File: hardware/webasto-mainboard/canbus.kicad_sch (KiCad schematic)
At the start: 17 parts, among them Q17 2N7002, Q18 2N7002, U10 MCP2557FD-xMF, U8 TCA9534, U9 MCP2517FD, X1 ASV-20.000MHZ-EJ-T

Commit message: Remove WiFi, plumb in the CANBus
- The next joy will be to remove the external I2C, and have all the
  sensors talk to us via CANBus as well.
- First I need to determine how to restructure to enumerate my sensors
- Nice thing is, the sensors will share an ID space across the bus
  (including LINBus, which will now need rework too)
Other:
- note added: "I2C Addr 0x20-27 We will use 27"
- note removed: "I2C Addr 0x38-3F We will use 3F"
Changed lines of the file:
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@@
     (stroke (width 0) (type default) (color 0 0 0 0))
   )
-  (text "I2C Addr 0x38-3F\nWe will use 3F" (at 61.087 182.753 0)
+  (text "I2C Addr 0x20-27\nWe will use 27" (at 61.087 182.753 0)
     (effects (font (size 1.27 1.27)) (justify left bottom))
   )

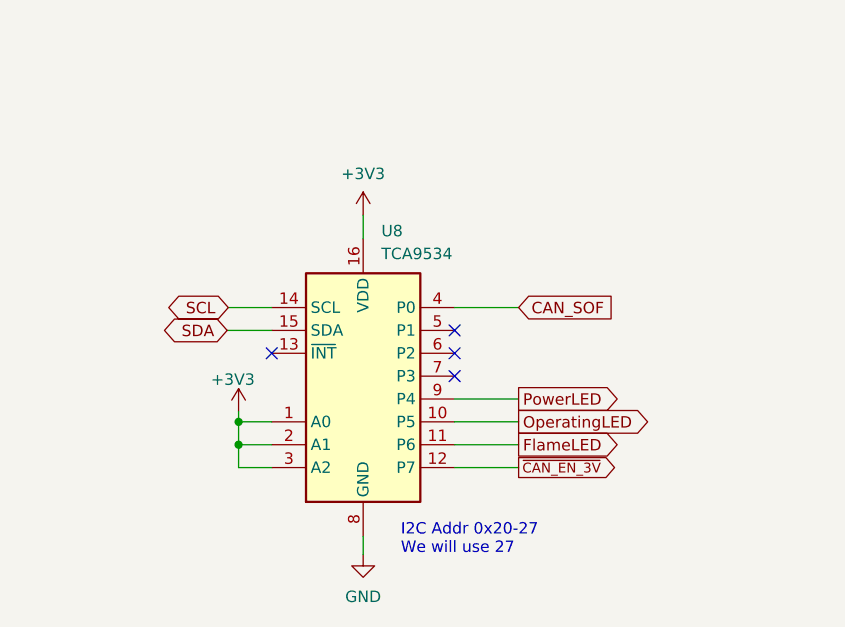
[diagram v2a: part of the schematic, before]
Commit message: Removing KLine and I2C from X1, reattaching the external IOs.
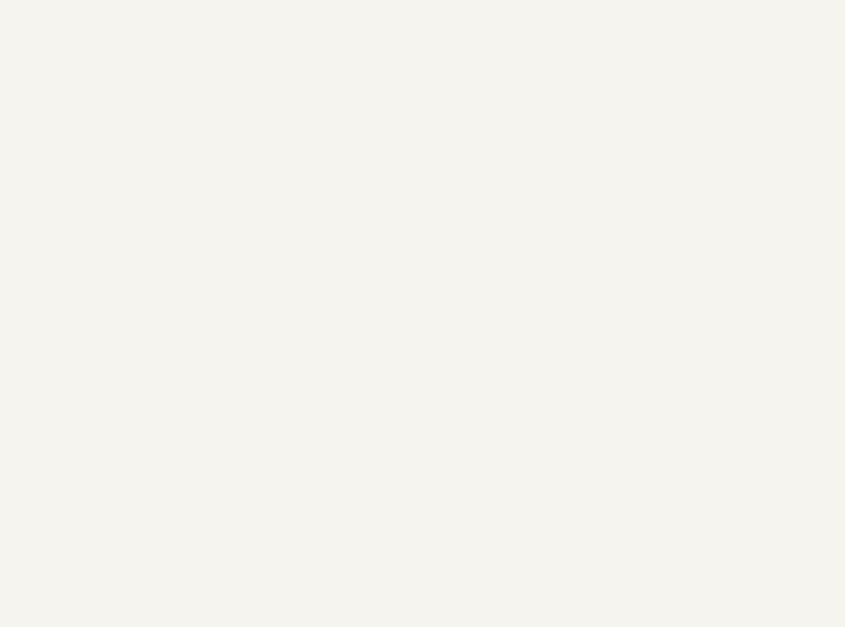
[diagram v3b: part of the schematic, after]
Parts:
- removed U8: TCA9534, Package_SO:TSSOP-16_4.4x5mm_P0.65mm, symbol Interface_Expansion:TCA9534
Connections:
- no-connect marks 7 -> 3
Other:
- note removed: "I2C Addr 0x20-27 We will use 27"
